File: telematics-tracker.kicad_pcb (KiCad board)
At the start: 4 copper layers, 82 x 62 mm, 216 parts, among them J1 WAFER-MX3.0-12PZZ, J2 B3B-XH-A, Q1 AM2390N-TP, Q10 MMBT3904, Q11 MMBT3904, Q12 MMBT3904, Q13 MMBT3906, Q14 MMBT3904, Q2 AM2390N-TP, Q3 AO3401A, Q4 MMBT3904, Q5 MMBT3904, Q6 MMBT3904, Q7 MMBT3904, Q8 MMBT3904, Q9 MMBT3904, U1 EC200UCNAA-N05-SGNSA, U2 AT32F403ACGT7, U3 QMI8658B, U4 SIT1051AT/3, U5 EG11752, U6 BQ25606RGER, U7 GD25Q64ESIGR, U8 TXB0104PWR, U9 ME6211C33M5G, X1 NANO-SIM, X2 MFF2-eSIM-pads, Y1 8MHz, Y2 32.768kHz

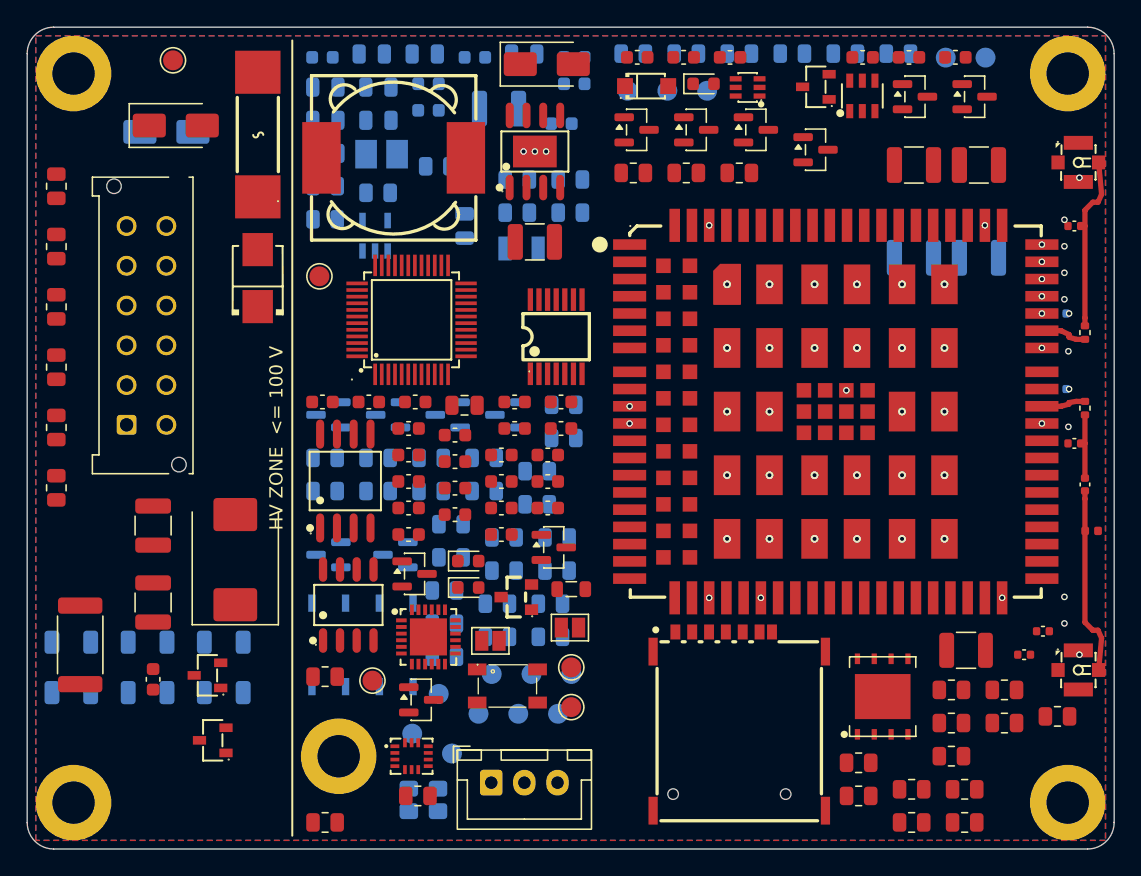
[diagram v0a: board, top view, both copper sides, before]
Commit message: hybrid cycle 1: unconnected=Found 0 violations Found 175 unconnected items Saved DRC Report to /tmp/claude-1000/-home-david-pcb/585b5aba-c6c8-4274-99b1-afe6f39de64b/tmp/cy1.rpt 175
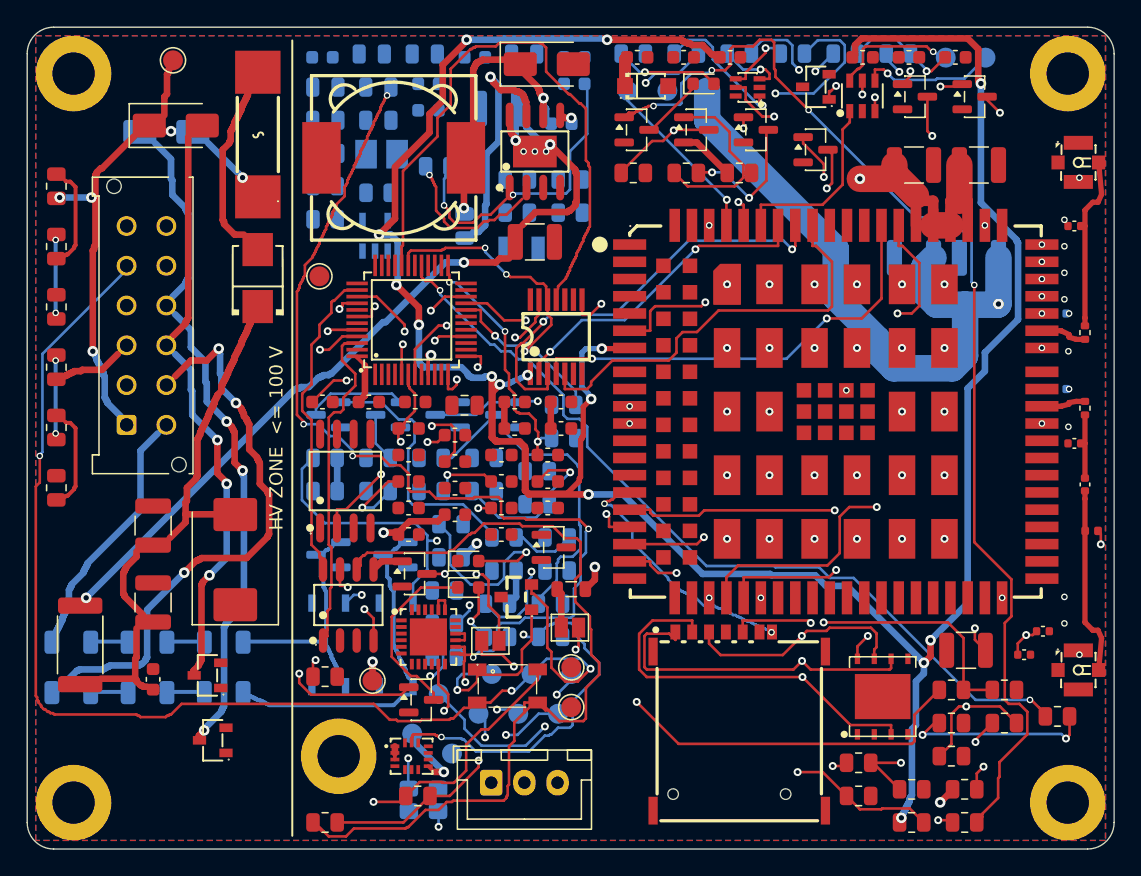
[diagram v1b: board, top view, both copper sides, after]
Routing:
- net /modem_rf/VDD_EXT_1V8: track 0.00 -> 206.5 mm, vias 0 -> 15
- net MODEM_STATUS: track 0.00 -> 132.9 mm, vias 0 -> 3
- net /io/CANL: track 0.00 -> 91.2 mm, vias 0 -> 3
- net /modem_rf/Q12_B: track 0.00 -> 86.3 mm, vias 0 -> 4
- net /power/VBAT_BT: track 0.00 -> 84.7 mm, vias 0 -> 6
- net /modem_rf/SIM_DATA: track 0.00 -> 84.3 mm, vias 0 -> 2
- net /modem_rf/SIM_CLK: track 0.00 -> 78.0 mm, vias 0 -> 2
- net MODEM_RESET: track 0.00 -> 74.5 mm, vias 0 -> 2
- net /modem_rf/USIM_VDD: track 0.00 -> 72.5 mm, vias 0 -> 3
- net /modem_rf/VBAT_MODEM: track 0.00 -> 71.2 mm, vias 0 -> 2
- net /modem_rf/SIM_RST: track 0.00 -> 67.3 mm, vias 0 -> 2
- net MODEM_PWR_EN: track 0.00 -> 64.5 mm, vias 0 -> 2
- net /io/CANL_T: track 0.00 -> 64.4 mm
- net /modem_rf/Q9_B: track 0.00 -> 63.7 mm, vias 0 -> 3
- net MODEM_PWRKEY: track 0.00 -> 63.0 mm, vias 0 -> 2
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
